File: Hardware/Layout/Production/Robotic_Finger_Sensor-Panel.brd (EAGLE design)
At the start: 106.4 x 98.3 mm, 513 parts, among them U1 VCNL4040, U10 MS5637, U11 VCNL4040, U12 MS5637, U13 VCNL4040, U14 MS5637, U15 VCNL4040, U16 MS5637, U17 VCNL4040, U18 MS5637, U19 VCNL4040, U2 VCNL4040, U20 MS5637, U21 VCNL4040, U22 MS5637, U23 VCNL4040, U24 MS5637, U25 VCNL4040, U26 MS5637, U27 VCNL4040, U28 MS5637, U29 VCNL4040, U3 MS5637, U30 MS5637, U31 VCNL4040, U32 MS5637, U33 VCNL4040, U34 MS5637, U35 VCNL4040, U36 MS5637, U37 VCNL4040, U38 MS5637, U39 VCNL4040, U4 MS5637, U40 MS5637, U41 VCNL4040, U42 MS5637, U43 VCNL4040, U44 MS5637, U45 VCNL4040, U46 MS5637, U47 VCNL4040, U48 MS5637, U49 VCNL4040, U5 VCNL4040, U50 MS5637, U51 VCNL4040, U52 MS5637, U53 VCNL4040, U54 MS5637, U55 VCNL4040, U56 MS5637, U57 VCNL4040, U58 MS5637, U59 VCNL4040, U6 MS5637, U60 MS5637, U7 VCNL4040, U8 MS5637, U9 VCNL4040

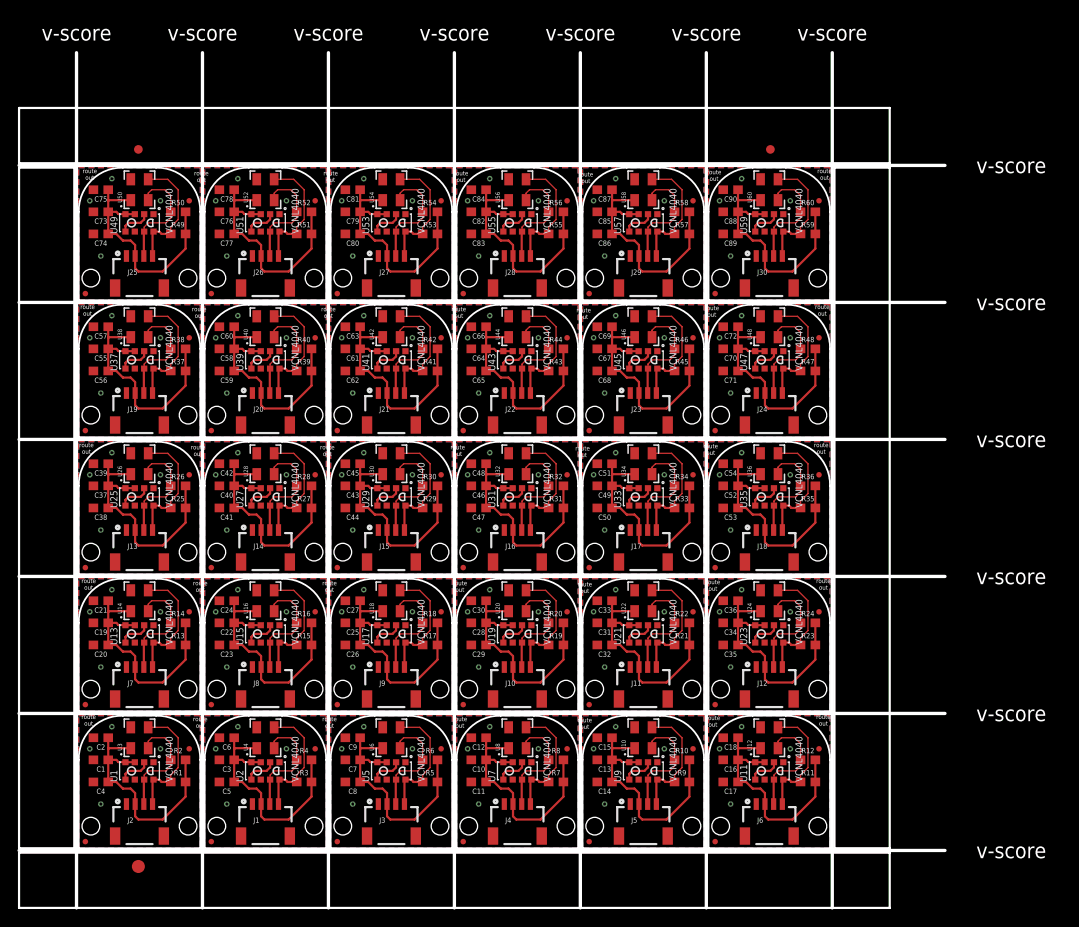
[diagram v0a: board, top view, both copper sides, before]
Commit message: Update to LPS25HB pressure sensor
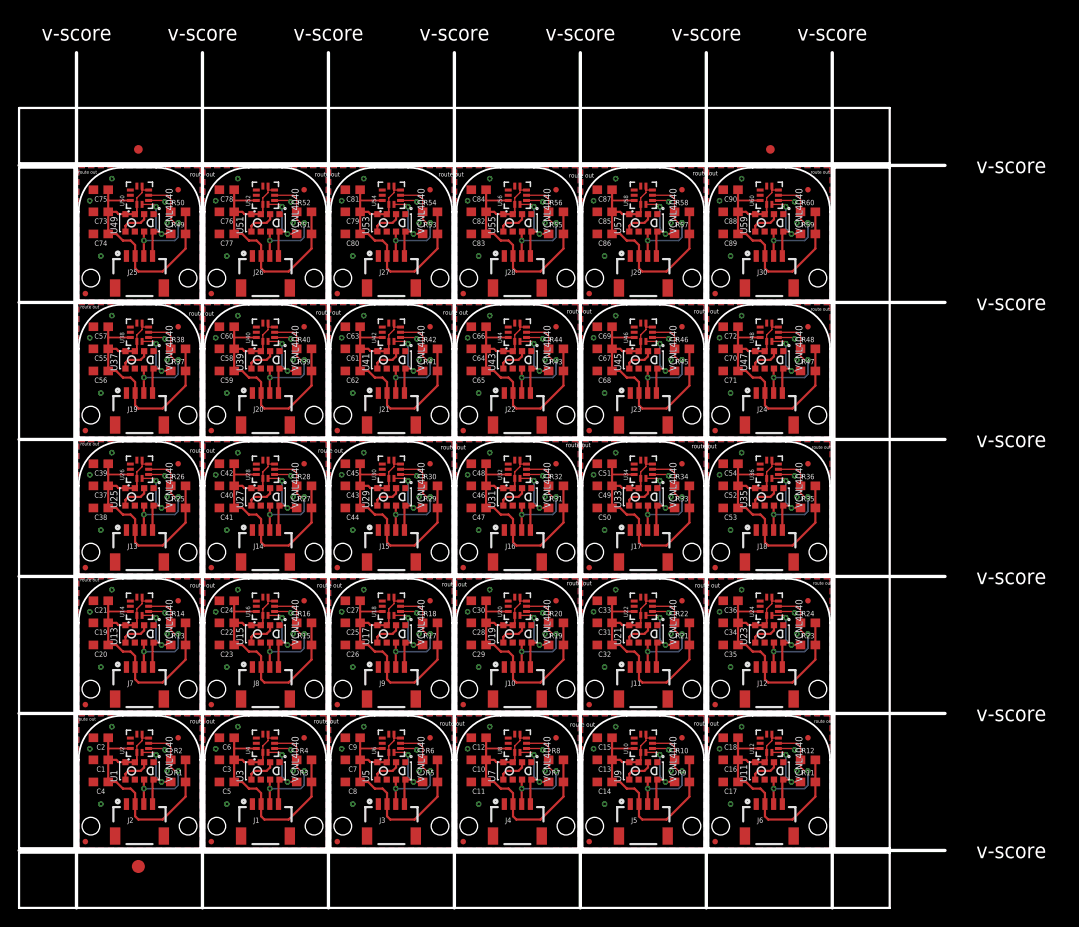
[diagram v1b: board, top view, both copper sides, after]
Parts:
- C1, C10, C13, C16, C19, C22, C25, C28, C3, C31, C34, C37, C40, C43, C46, C49, C52, C55, C58, C61, C64, C67, C7, C70, C73, C76, C79, C82, C85, C88: value 2.2uF -> 4.7uF
- U$10: device buzzard_labels:SENSOR5 -> Labels-0_04:(QWIIC)
- U$102, U$109, U$116, U$123, U$130, U$137, U$144, U$151, U$158, U$165, U$172, U$179, U$18, U$186, U$193, U$200, U$207, U$25, U$32, U$39, U$46, U$53, U$60, U$67, U$74, U$81, U$88, U$95: device buzzard_labels:ROBOTIC3 -> Labels-0_04:(QWIIC)
- U$103, U$110, U$117, U$12, U$124, U$131, U$138, U$145, U$152, U$159, U$166, U$173, U$180, U$187, U$19, U$194, U$201, U$208, U$26, U$33, U$40, U$47, U$54, U$61, U$68, U$75, U$82, U$89, U$96: device buzzard_labels:FINGER4 -> buzzard_labels:ROBOTIC0
- U$104, U$111, U$118, U$125, U$13, U$132, U$139, U$146, U$153, U$160, U$167, U$174, U$181, U$188, U$195, U$20, U$202, U$209, U$27, U$34, U$41, U$48, U$55, U$62, U$69, U$76, U$83, U$90, U$97: device buzzard_labels:SENSOR5 -> buzzard_labels:SENSOR2
- U$105, U$112, U$119, U$126, U$133, U$14, U$140, U$147, U$154, U$161, U$168, U$175, U$182, U$189, U$196, U$203, U$21, U$210, U$28, U$35, U$42, U$49, U$56, U$63, U$70, U$77, U$84, U$91, U$98: device Labels-0_04:(QWIIC) -> buzzard_labels (1):FINGER0
- U$5: value (none) -> STAND-OFF; device buzzard_labels:ROBOTIC3 -> SparkX:STAND-OFF-#2
- U$6: value STAND-OFF -> (none); device SparkX:STAND-OFF-#2 -> buzzard_labels:ROBOTIC0
- U$7: value STAND-OFF -> (none); device SparkX:STAND-OFF-#2 -> buzzard_labels:SENSOR2
- U$8: value (none) -> STAND-OFF; device buzzard_labels:FINGER4 -> SparkX:STAND-OFF-#2
- U$9: device buzzard_labels:ROBOTIC3 -> buzzard_labels (1):FINGER0
- U10, U12, U14, U16, U18, U20, U22, U24, U26, U28, U30, U32, U34, U36, U38, U4, U40, U42, U44, U46, U48, U50, U52, U54, U56, U58, U6, U60, U8: value MS5637 -> LPS25HB; device MS5637:MS5637 -> LPS25HB:LPS25HB
- U2: value VCNL4040 -> LPS25HB; device SparkX:VCNL4040 -> LPS25HB:LPS25HB
- U3: value MS5637 -> VCNL4040; device MS5637:MS5637 -> SparkX:VCNL4040
- moved U$8 17.3 mm to (27.1, 2.54), flipped to the top
- moved U$7 16.7 mm to (11.2, 7.75), flipped to the bottom
- moved U$9 15.1 mm to (10.8, 9.40)
- moved U3 15.0 mm to (21.5, 8.89)
- moved U2 14.8 mm to (6.99, 12.1)
- moved U$10 13.6 mm to (24.3, 3.43)
- moved U$6 9.66 mm to (11.3, 11.0), flipped to the bottom
- moved U$5 9.44 mm to (15.9, 2.54), flipped to the top
- moved U$102 7.52 mm to (38.7, 34.9)
- moved U$109 7.52 mm to (53.2, 34.9)
- moved U$116 7.52 mm to (67.7, 34.9)
- moved U$123 7.52 mm to (82.2, 34.9)
- moved U$130 7.52 mm to (9.78, 50.7)
- moved U$144 7.52 mm to (38.7, 50.7)
- moved U$151 7.52 mm to (53.2, 50.7)
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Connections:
- removed net SCL: J2.4, R1.1, U1.8, U3.3
- removed net SCL1: J1.4, R3.1, U2.8, U4.3
- removed net SCL10: J11.4, R21.1, U21.8, U22.3
- removed net SCL11: J12.4, R23.1, U23.8, U24.3
- removed net SCL12: J13.4, R25.1, U25.8, U26.3
- removed net SCL13: J14.4, R27.1, U27.8, U28.3
- removed net SCL14: J15.4, R29.1, U29.8, U30.3
- removed net SCL15: J16.4, R31.1, U31.8, U32.3
- removed net SCL16: J17.4, R33.1, U33.8, U34.3
- removed net SCL17: J18.4, R35.1, U35.8, U36.3
- removed net SCL18: J19.4, R37.1, U37.8, U38.3
- removed net SCL19: J20.4, R39.1, U39.8, U40.3
- removed net SCL2: J3.4, R5.1, U5.8, U6.3
- removed net SCL20: J21.4, R41.1, U41.8, U42.3
- removed net SCL21: J22.4, R43.1, U43.8, U44.3
- removed net SCL22: J23.4, R45.1, U45.8, U46.3
- removed net SCL23: J24.4, R47.1, U47.8, U48.3
- removed net SCL24: J25.4, R49.1, U49.8, U50.3
- removed net SCL25: J26.4, R51.1, U51.8, U52.3
- removed net SCL26: J27.4, R53.1, U53.8, U54.3
- removed net SCL27: J28.4, R55.1, U55.8, U56.3
- removed net SCL28: J29.4, R57.1, U57.8, U58.3
- removed net SCL29: J30.4, R59.1, U59.8, U60.3
- removed net SCL3: J4.4, R7.1, U7.8, U8.3
- removed net SCL4: J5.4, R9.1, U10.3, U9.8
- removed net SCL5: J6.4, R11.1, U11.8, U12.3
- removed net SCL6: J7.4, R13.1, U13.8, U14.3
- removed net SCL7: J8.4, R15.1, U15.8, U16.3
- removed net SCL8: J9.4, R17.1, U17.8, U18.3
- removed net SCL9: J10.4, R19.1, U19.8, U20.3
- removed net SDA: J2.3, R2.1, U1.7, U3.2
- removed net SDA1: J1.3, R4.1, U2.7, U4.2
- removed net SDA10: J11.3, R22.1, U21.7, U22.2
- removed net SDA11: J12.3, R24.1, U23.7, U24.2
- removed net SDA12: J13.3, R26.1, U25.7, U26.2
- removed net SDA13: J14.3, R28.1, U27.7, U28.2
- removed net SDA14: J15.3, R30.1, U29.7, U30.2
- removed net SDA15: J16.3, R32.1, U31.7, U32.2
- removed net SDA16: J17.3, R34.1, U33.7, U34.2
- removed net SDA17: J18.3, R36.1, U35.7, U36.2
- removed net SDA18: J19.3, R38.1, U37.7, U38.2
- removed net SDA19: J20.3, R40.1, U39.7, U40.2
- removed net SDA2: J3.3, R6.1, U5.7, U6.2
- removed net SDA20: J21.3, R42.1, U41.7, U42.2
- removed net SDA21: J22.3, R44.1, U43.7, U44.2
- removed net SDA22: J23.3, R46.1, U45.7, U46.2
- removed net SDA23: J24.3, R48.1, U47.7, U48.2
- removed net SDA24: J25.3, R50.1, U49.7, U50.2
- removed net SDA25: J26.3, R52.1, U51.7, U52.2
- removed net SDA26: J27.3, R54.1, U53.7, U54.2
- removed net SDA27: J28.3, R56.1, U55.7, U56.2
- removed net SDA28: J29.3, R58.1, U57.7, U58.2
- removed net SDA29: J30.3, R60.1, U59.7, U60.2
- removed net SDA3: J4.3, R8.1, U7.7, U8.2
- removed net SDA4: J5.3, R10.1, U10.2, U9.7
- removed net SDA5: J6.3, R12.1, U11.7, U12.2
- removed net SDA6: J7.3, R14.1, U13.7, U14.2
- removed net SDA7: J8.3, R16.1, U15.7, U16.2
- removed net SDA8: J9.3, R18.1, U17.7, U18.2
- removed net SDA9: J10.3, R20.1, U19.7, U20.2
- new net SCL/SCK: J2.4, R1.1, U1.8, U2.2
- new net SCL/SCK1: J1.4, R3.1, U3.8, U4.2
- new net SCL/SCK10: J11.4, R21.1, U21.8, U22.2
- new net SCL/SCK11: J12.4, R23.1, U23.8, U24.2
- new net SCL/SCK12: J13.4, R25.1, U25.8, U26.2
- new net SCL/SCK13: J14.4, R27.1, U27.8, U28.2
- new net SCL/SCK14: J15.4, R29.1, U29.8, U30.2
- new net SCL/SCK15: J16.4, R31.1, U31.8, U32.2
- new net SCL/SCK16: J17.4, R33.1, U33.8, U34.2
- new net SCL/SCK17: J18.4, R35.1, U35.8, U36.2
- new net SCL/SCK18: J19.4, R37.1, U37.8, U38.2
- new net SCL/SCK19: J20.4, R39.1, U39.8, U40.2
- new net SCL/SCK2: J3.4, R5.1, U5.8, U6.2
- new net SCL/SCK20: J21.4, R41.1, U41.8, U42.2
- new net SCL/SCK21: J22.4, R43.1, U43.8, U44.2
- new net SCL/SCK22: J23.4, R45.1, U45.8, U46.2
- new net SCL/SCK23: J24.4, R47.1, U47.8, U48.2
- new net SCL/SCK24: J25.4, R49.1, U49.8, U50.2
- new net SCL/SCK25: J26.4, R51.1, U51.8, U52.2
- new net SCL/SCK26: J27.4, R53.1, U53.8, U54.2
- new net SCL/SCK27: J28.4, R55.1, U55.8, U56.2
- new net SCL/SCK28: J29.4, R57.1, U57.8, U58.2
- new net SCL/SCK29: J30.4, R59.1, U59.8, U60.2
- new net SCL/SCK3: J4.4, R7.1, U7.8, U8.2
- new net SCL/SCK4: J5.4, R9.1, U10.2, U9.8
- new net SCL/SCK5: J6.4, R11.1, U11.8, U12.2
- new net SCL/SCK6: J7.4, R13.1, U13.8, U14.2
- new net SCL/SCK7: J8.4, R15.1, U15.8, U16.2
- new net SCL/SCK8: J9.4, R17.1, U17.8, U18.2
- new net SCL/SCK9: J10.4, R19.1, U19.8, U20.2
- new net SDA/MOSI: J2.3, R2.1, U1.7, U2.4
- new net SDA/MOSI1: J1.3, R4.1, U3.7, U4.4
- new net SDA/MOSI10: J11.3, R22.1, U21.7, U22.4
- new net SDA/MOSI11: J12.3, R24.1, U23.7, U24.4
- new net SDA/MOSI12: J13.3, R26.1, U25.7, U26.4
- new net SDA/MOSI13: J14.3, R28.1, U27.7, U28.4
- new net SDA/MOSI14: J15.3, R30.1, U29.7, U30.4
- new net SDA/MOSI15: J16.3, R32.1, U31.7, U32.4
- new net SDA/MOSI16: J17.3, R34.1, U33.7, U34.4
- new net SDA/MOSI17: J18.3, R36.1, U35.7, U36.4
- new net SDA/MOSI18: J19.3, R38.1, U37.7, U38.4
- new net SDA/MOSI19: J20.3, R40.1, U39.7, U40.4
- new net SDA/MOSI2: J3.3, R6.1, U5.7, U6.4
- new net SDA/MOSI20: J21.3, R42.1, U41.7, U42.4
- new net SDA/MOSI21: J22.3, R44.1, U43.7, U44.4
- new net SDA/MOSI22: J23.3, R46.1, U45.7, U46.4
- new net SDA/MOSI23: J24.3, R48.1, U47.7, U48.4
- new net SDA/MOSI24: J25.3, R50.1, U49.7, U50.4
- new net SDA/MOSI25: J26.3, R52.1, U51.7, U52.4
- new net SDA/MOSI26: J27.3, R54.1, U53.7, U54.4
- new net SDA/MOSI27: J28.3, R56.1, U55.7, U56.4
- new net SDA/MOSI28: J29.3, R58.1, U57.7, U58.4
- new net SDA/MOSI29: J30.3, R60.1, U59.7, U60.4
- new net SDA/MOSI3: J4.3, R8.1, U7.7, U8.4
- new net SDA/MOSI4: J5.3, R10.1, U10.4, U9.7
- new net SDA/MOSI5: J6.3, R12.1, U11.7, U12.4
- new net SDA/MOSI6: J7.3, R14.1, U13.7, U14.4
- new net SDA/MOSI7: J8.3, R16.1, U15.7, U16.4
- new net SDA/MOSI8: J9.3, R18.1, U17.7, U18.4
- new net SDA/MOSI9: J10.3, R20.1, U19.7, U20.4
- net 3.3V: now also U2.1, U2.10, U2.5, U2.6; no longer U3.1
- net 3.3V1: now also U3.3, U3.4, U4.10, U4.5, U4.6; no longer U2.3, U2.4
- net 3.3V10: now also U22.10, U22.5, U22.6
- net 3.3V11: now also U24.10, U24.5, U24.6
- net 3.3V12: now also U26.10, U26.5, U26.6
- net 3.3V13: now also U28.10, U28.5, U28.6
- net 3.3V14: now also U30.10, U30.5, U30.6
- net 3.3V15: now also U32.10, U32.5, U32.6
- net 3.3V16: now also U34.10, U34.5, U34.6
- net 3.3V17: now also U36.10, U36.5, U36.6
- net 3.3V18: now also U38.10, U38.5, U38.6
- net 3.3V19: now also U40.10, U40.5, U40.6
- net 3.3V2: now also U6.10, U6.5, U6.6
- net 3.3V20: now also U42.10, U42.5, U42.6
- net 3.3V21: now also U44.10, U44.5, U44.6
- net 3.3V22: now also U46.10, U46.5, U46.6
- net 3.3V23: now also U48.10, U48.5, U48.6
- net 3.3V24: now also U50.10, U50.5, U50.6
- net 3.3V25: now also U52.10, U52.5, U52.6
- net 3.3V26: now also U54.10, U54.5, U54.6
- net 3.3V27: now also U56.10, U56.5, U56.6
- net 3.3V28: now also U58.10, U58.5, U58.6
- net 3.3V29: now also U60.10, U60.5, U60.6
- net 3.3V3: now also U8.10, U8.5, U8.6
- net 3.3V4: now also U10.10, U10.5, U10.6
- net 3.3V5: now also U12.10, U12.5, U12.6
- net 3.3V6: now also U14.10, U14.5, U14.6
- net 3.3V7: now also U16.10, U16.5, U16.6
- net 3.3V8: now also U18.10, U18.5, U18.6
- net 3.3V9: now also U20.10, U20.5, U20.6
- net GND: now also U2.3, U2.8, U2.9; no longer U3.4
- net GND1: now also U3.1, U4.3, U4.8, U4.9; no longer U2.1, U4.4
- net GND10: now also U22.3, U22.8, U22.9; no longer U22.4
- net GND11: now also U24.3, U24.8, U24.9; no longer U24.4
- net GND12: now also U26.3, U26.8, U26.9; no longer U26.4
- net GND13: now also U28.3, U28.8, U28.9; no longer U28.4
- net GND14: now also U30.3, U30.8, U30.9; no longer U30.4
- net GND15: now also U32.3, U32.8, U32.9; no longer U32.4
- net GND16: now also U34.3, U34.8, U34.9; no longer U34.4
- net GND17: now also U36.3, U36.8, U36.9; no longer U36.4
- net GND18: now also U38.3, U38.8, U38.9; no longer U38.4
- net GND19: now also U40.3, U40.8, U40.9; no longer U40.4
- net GND2: now also U6.3, U6.8, U6.9; no longer U6.4
- net GND20: now also U42.3, U42.8, U42.9; no longer U42.4
- net GND21: now also U44.3, U44.8, U44.9; no longer U44.4
- net GND22: now also U46.3, U46.8, U46.9; no longer U46.4
- net GND23: now also U48.3, U48.8, U48.9; no longer U48.4
- net GND24: now also U50.3, U50.8, U50.9; no longer U50.4
- net GND25: now also U52.3, U52.8, U52.9; no longer U52.4
- net GND26: now also U54.3, U54.8, U54.9; no longer U54.4
- net GND27: now also U56.3, U56.8, U56.9; no longer U56.4
- net GND28: now also U58.3, U58.8, U58.9; no longer U58.4
- net GND29: now also U60.3, U60.8, U60.9; no longer U60.4
- net GND3: now also U8.3, U8.8, U8.9; no longer U8.4
- net GND4: now also U10.3, U10.8, U10.9; no longer U10.4
- net GND5: now also U12.3, U12.8, U12.9; no longer U12.4
- net GND6: now also U14.3, U14.8, U14.9; no longer U14.4
- net GND7: now also U16.3, U16.8, U16.9; no longer U16.4
- net GND8: now also U18.3, U18.8, U18.9; no longer U18.4
- net GND9: now also U20.3, U20.8, U20.9; no longer U20.4
- net N$2: now also U3.2, U3.5; no longer U2.2, U2.5
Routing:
- net SDA/MOSI24: track 0.00 -> 14.6 mm, vias 0 -> 2
- net SDA/MOSI27: track 0.00 -> 14.6 mm, vias 0 -> 2
- net SDA/MOSI26: track 0.00 -> 14.6 mm, vias 0 -> 2
- net SDA/MOSI25: track 0.00 -> 14.6 mm, vias 0 -> 2
- net SDA/MOSI12: track 0.00 -> 14.6 mm, vias 0 -> 2
- net SDA/MOSI21: track 0.00 -> 14.6 mm, vias 0 -> 2
- net SDA/MOSI20: track 0.00 -> 14.6 mm, vias 0 -> 2
- net SDA/MOSI13: track 0.00 -> 14.6 mm, vias 0 -> 2
- net SDA/MOSI9: track 0.00 -> 14.6 mm, vias 0 -> 2
- net SDA/MOSI8: track 0.00 -> 14.6 mm, vias 0 -> 2
- net SDA/MOSI7: track 0.00 -> 14.6 mm, vias 0 -> 2
- net SDA/MOSI6: track 0.00 -> 14.6 mm, vias 0 -> 2
- net SDA/MOSI19: track 0.00 -> 14.6 mm, vias 0 -> 2
- net SDA/MOSI18: track 0.00 -> 14.6 mm, vias 0 -> 2
- net SDA/MOSI15: track 0.00 -> 14.6 mm, vias 0 -> 2
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
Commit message: Updating examples to use modern libraries
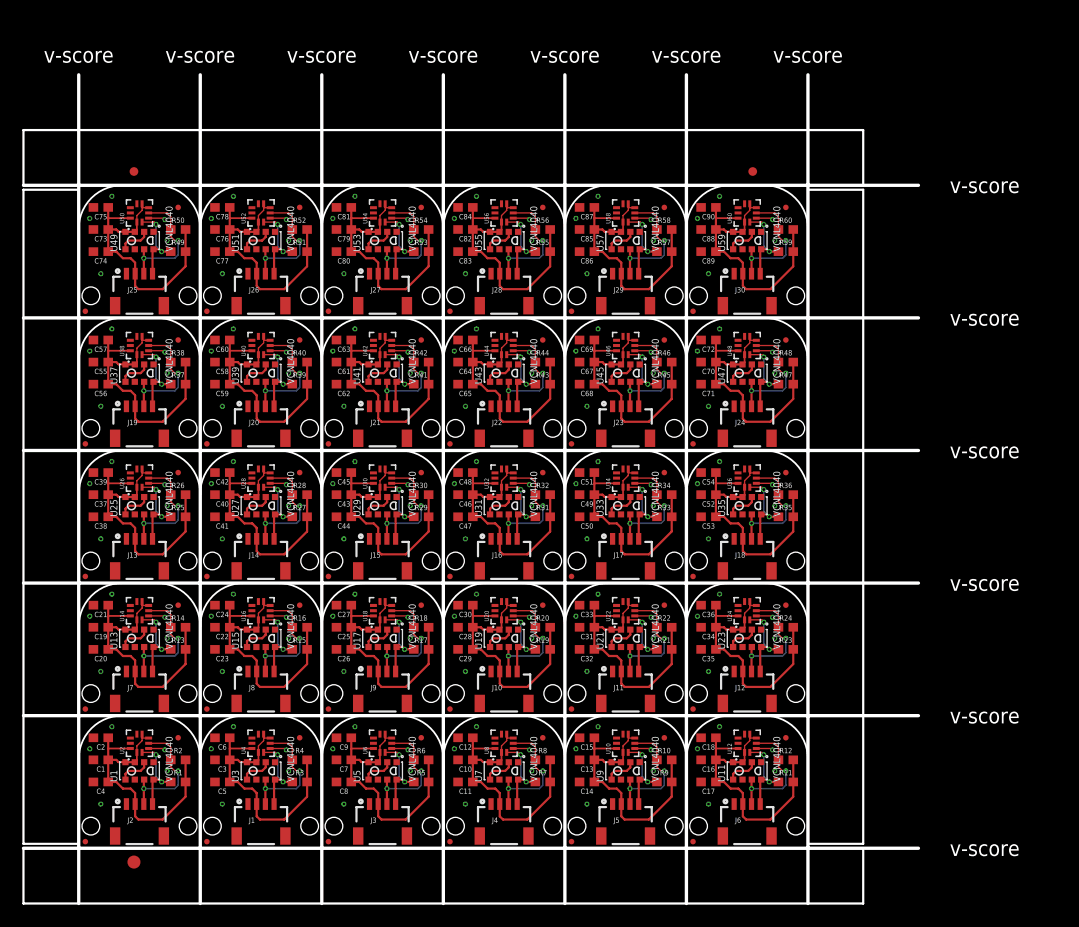
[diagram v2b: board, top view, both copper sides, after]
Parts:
- moved U$209 3.25 mm to (81.0, 68.7)
- moved U59 3.25 mm to (76.8, 69.8)
- moved U$204 3.25 mm to (76.8, 62.2)
- moved C88 3.25 mm to (72.4, 71.1)
- moved C89 3.25 mm to (72.4, 68.6)
- moved C90 3.25 mm to (72.4, 73.7)
- moved E$2 3.25 mm to (77.5, 77.8)
- moved FD60 3.25 mm to (70.6, 61.7)
- moved J30 3.25 mm to (76.8, 66.0)
- moved U$205 3.25 mm to (71.2, 63.5)
- moved U$210 3.25 mm to (80.6, 70.4)
- moved U60 3.25 mm to (76.8, 73.0)
- moved U$207 3.25 mm to (79.6, 64.4)
- moved FD59 3.25 mm to (81.3, 73.7)
- moved R59 3.25 mm to (81.3, 68.6)
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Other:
- board size 106.4 x 98.3 mm -> 102.9 x 95.2 mm
- board text removed: "route out"
